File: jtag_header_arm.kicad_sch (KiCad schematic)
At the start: 3 parts, among them J5 02x10_2.54mm_Header_Odd_Even

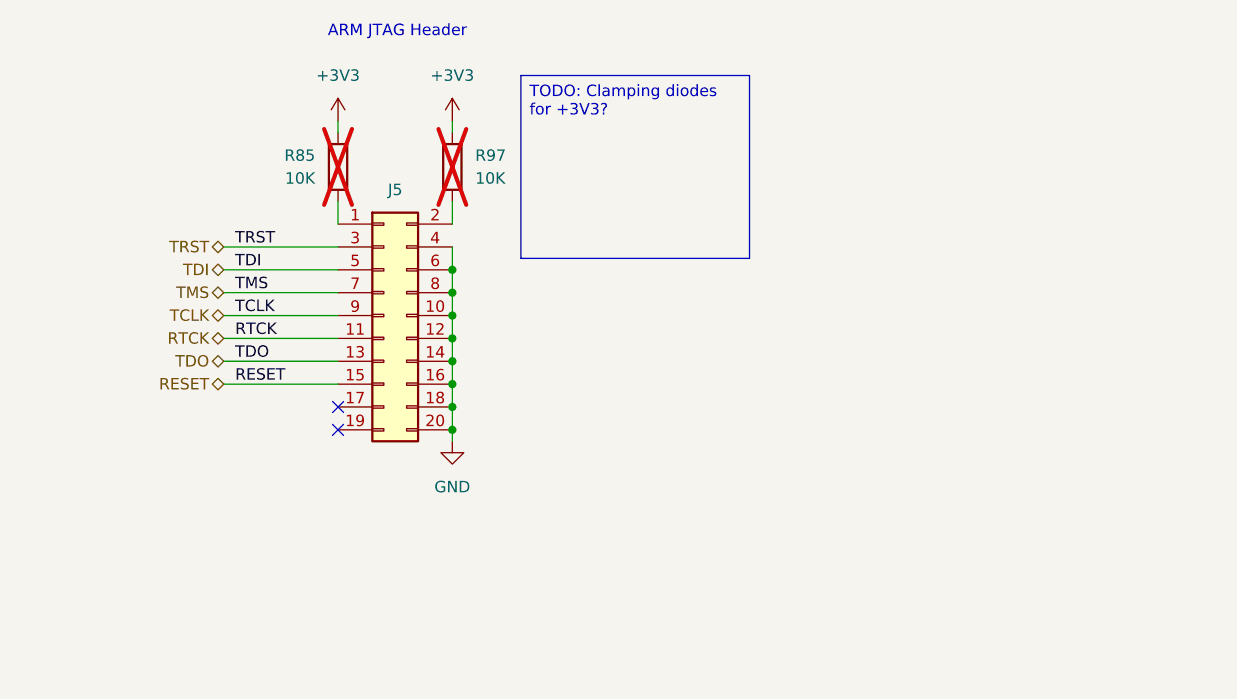
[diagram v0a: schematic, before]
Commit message: connects JTAG header. Refs: #1
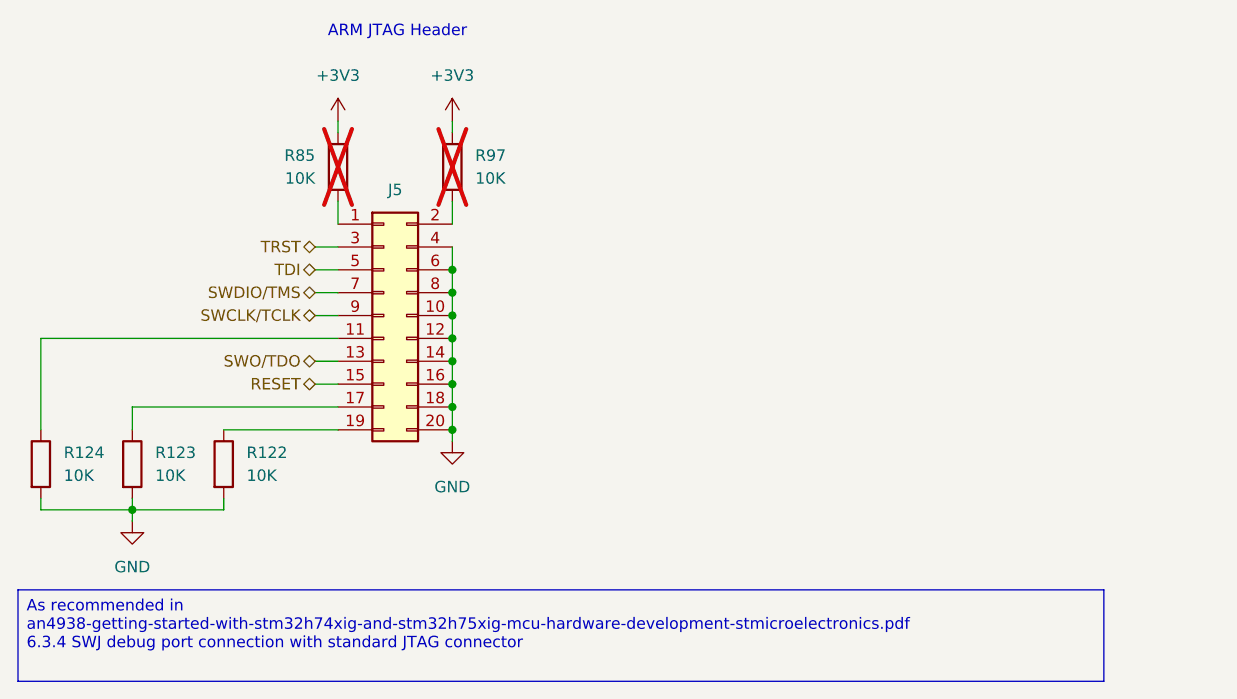
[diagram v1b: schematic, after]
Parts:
- added R122, R123, R124: 10K, KL_Footprints:R_0603, symbol KL_R:R_10K_100mW_5_0603
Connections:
- net GND: now also R122.2, R123.2, R124.2
- net at J5.17 (Pin_17): now also R123.1
- net at J5.19 (Pin_19): now also R122.1
- net RTCK: no longer names the net of J5.11 (Pin_11)
- net RTCK: now also R124.1
- net TCLK renamed SWCLK/TCLK
- net TDO renamed SWO/TDO
- net TMS renamed SWDIO/TMS
- no-connect marks 2 -> 0

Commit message: fixes duplicate R85. Refs: #1
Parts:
- removed R85: 10K, KL_Footprints:C_0603, symbol KL_R:R_10K_100mW_5_0603
- added R109: 10K, KL_Footprints:C_0603, symbol KL_R:R_10K_100mW_5_0603
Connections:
- net +3V3: now also R109.2
- net at J5.1 (Pin_1): now also R109.1
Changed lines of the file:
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@@
+	)
+	(symbol
+		(lib_id "KL_R:R_10K_100mW_5_0603")
+		(at 127 57.15 180)
+		(unit 1)
+		(exclude_from_sim no)
+		(in_bom no)
+		(on_board yes)
+		(dnp yes)
+		(fields_autoplaced yes)
+		(property "Reference" "R109"
+			(at 124.46 55.8799 0)
+			(effects
+				(font
+					(size 1.27 1.27)
+				)
+				(justify left)
+			)
+		)
+		(property "Value" "10K"
+			(at 124.46 58.4199 0)
+			(effects
+				(font
+					(size 1.27 1.27)
+				)
+				(justify left)
+			)
+		)
+		(property "Footprint" "KL_Footprints:C_0603"
+			(at 128.778 57.15 90)
+			(effects
+				(font
+					(size 1.27 1.27)
+				)
+				(hide yes)
+			)
+		)
+		(property "Datasheet" "~"
+			(at 127 57.15 0)
+			(effects
+				(font
+					(size 1.27 1.27)
+				)
+				(hide yes)
+			)
+		)
+		(property "Description" "Resistor"
+			(at 127 57.15 0)
+			(effects
+				(font
+					(size 1.27 1.27)
+				)
+				(hide yes)
+			)
+		)
+		(property "Power" "100mW"
+			(at 127 57.15 0)
+			(effects
+				(font
+					(size 1.27 1.27)
+				)
+				(hide yes)
+			)
+		)
+		(property "Tolerance" "5%"
+			(at 127 57.15 0)
+			(effects
+				(font
+					(size 1.27 1.27)
+				)
+				(hide yes)
+			)
+		)
+		(property "Mouser" "71-CRCW060310K0JNEC"
+			(at 127 57.15 0)
+			(effects
+				(font
+					(size 1.27 1.27)
+				)
+				(hide yes)
+			)
+		)
+		(property "Digikey" "541-CRCW060310K0JNECCT-ND"
+			(at 127 57.15 0)
+			(effects
+				(font
+					(size 1.27 1.27)
+				)
+				(hide yes)
+			)
+		)
+		(property "LCSC" "C4195694"
+			(at 127 57.15 0)
+			(effects
+				(font
+					(size 1.27 1.27)
+				)
+				(hide yes)
+			)
+		)
+		(property "Package (in)" "0603"
+			(at 127 57.15 0)
+			(effects
+				(font
+					(size 1.27 1.27)
+				)
+				(hide yes)
+			)
+		)
+		(property "Farnell" ""
+			(at 127 57.15 0)
+			(effects
+				(font
+					(size 1.27 1.27)
+				)
+				(hide yes)
+			)
+		)
+		(pin "1"
+		)
+		(pin "2"
+		)
+		(instances
+			(project "shish-lan"
+				(path "/d4536448-b109-4159-96e2-3dc21baf2d6e/06488c82-a47f-4277-b0ee-3bd211d8922a/54dd0313-e11b-4c5a-bb43-942dea0cd180"
+					(reference "R109")
+					(unit 1)
+				)
+			)
+		)
 	)
 	(symbol
@@
 					(unit 1)
 				)
-			)
-		)
-	)
-	(symbol
-		(lib_id "KL_R:R_10K_100mW_5_0603")
-		(at 127 57.15 180)
-		(unit 1)
-		(exclude_from_sim no)
-		(in_bom no)
-		(on_board yes)
-		(dnp yes)
-		(fields_autoplaced yes)
-		(property "Reference" "R85"
-			(at 124.46 55.8799 0)
-			(effects
-				(font
-					(size 1.27 1.27)
-				)
-				(justify left)
-			)
-		)
-		(property "Value" "10K"
-			(at 124.46 58.4199 0)
-			(effects
-				(font
-					(size 1.27 1.27)
-				)
-				(justify left)
-			)
-		)
-		(property "Footprint" "KL_Footprints:C_0603"
-			(at 128.778 57.15 90)
-			(effects
-				(font
-					(size 1.27 1.27)
-				)
-				(hide yes)
-			)
-		)
-		(property "Datasheet" "~"
-			(at 127 57.15 0)
-			(effects
-				(font
-					(size 1.27 1.27)
-				)
-				(hide yes)
-			)
-		)
-		(property "Description" "Resistor"
-			(at 127 57.15 0)
-			(effects
-				(font
-					(size 1.27 1.27)
-				)
-				(hide yes)
-			)
-		)
-		(property "Power" "100mW"
-			(at 127 57.15 0)
-			(effects
-				(font
-					(size 1.27 1.27)
-				)
-				(hide yes)
-			)
-		)
-		(property "Tolerance" "5%"
-			(at 127 57.15 0)
-			(effects
-				(font
-					(size 1.27 1.27)
-				)
-				(hide yes)
-			)
-		)
-		(property "Mouser" "71-CRCW060310K0JNEC"
-			(at 127 57.15 0)
-			(effects
-				(font
-					(size 1.27 1.27)
-				)
-				(hide yes)
-			)
-		)
-		(property "Digikey" "541-CRCW060310K0JNECCT-ND"
-			(at 127 57.15 0)
-			(effects
-				(font
-					(size 1.27 1.27)
-				)
-				(hide yes)
-			)
-		)
-		(property "LCSC" "C4195694"
-			(at 127 57.15 0)
-			(effects
-				(font
-					(size 1.27 1.27)
-				)
-				(hide yes)
-			)
-		)
-		(property "Package (in)" "0603"
-			(at 127 57.15 0)
-			(effects
-				(font
-					(size 1.27 1.27)
-				)
-				(hide yes)
-			)
-		)
-		(property "Farnell" ""
-			(at 127 57.15 0)
-			(effects
-				(font
-					(size 1.27 1.27)
-				)
-				(hide yes)
-			)
-		)
-		(pin "1"
-		)
-		(pin "2"
-		)
-		(instances
-			(project "shish-lan"
-				(path "/d4536448-b109-4159-96e2-3dc21baf2d6e/06488c82-a47f-4277-b0ee-3bd211d8922a/54dd0313-e11b-4c5a-bb43-942dea0cd180"
-					(reference "R85")
-					(unit 1)
-				)

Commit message: fixes ERC errors in DC/DC converters
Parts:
- R109, R97: footprint KL_Footprints:C_0603 -> KL_Footprints:R_0603; now in the parts list
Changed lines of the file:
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@@
 	)
 	(symbol
-		(lib_name "R_10K_100mW_5_0603_1")
 		(lib_id "KL_R:R_10K_100mW_5_0603")
 		(at 104.14 90.17 0)
@@
 	)
 	(symbol
-		(lib_name "R_10K_100mW_5_0603_1")
 		(lib_id "KL_R:R_10K_100mW_5_0603")
 		(at 93.98 90.17 0)
@@
 		(unit 1)
 		(exclude_from_sim no)
-		(in_bom no)
+		(in_bom yes)
 		(on_board yes)
 		(dnp yes)
 		(fields_autoplaced yes)
 		(property "Reference" "R109"
-			(at 124.46 55.8799 0)
-			(effects
-				(font
-					(size 1.27 1.27)
-				)
-				(justify left)
+			(at 129.54 55.8799 0)
+			(effects
+				(font
+					(size 1.27 1.27)
+				)
+				(justify right)
 			)
 		)
 		(property "Value" "10K"
-			(at 124.46 58.4199 0)
-			(effects
-				(font
-					(size 1.27 1.27)
-				)
-				(justify left)
-			)
-		)
-		(property "Footprint" "KL_Footprints:C_0603"
+			(at 129.54 58.4199 0)
+			(effects
+				(font
+					(size 1.27 1.27)
+				)
+				(justify right)
+			)
+		)
+		(property "Footprint" "KL_Footprints:R_0603"
 			(at 128.778 57.15 90)
 			(effects
@@
 	)
 	(symbol
-		(lib_name "R_10K_100mW_5_0603_1")
 		(lib_id "KL_R:R_10K_100mW_5_0603")
 		(at 114.3 90.17 0)
@@
 		(unit 1)
 		(exclude_from_sim no)
-		(in_bom no)
+		(in_bom yes)
 		(on_board yes)
 		(dnp yes)
@@
 			)
 		)
-		(property "Footprint" "KL_Footprints:C_0603"
+		(property "Footprint" "KL_Footprints:R_0603"
 			(at 141.478 57.15 90)
 			(effects
